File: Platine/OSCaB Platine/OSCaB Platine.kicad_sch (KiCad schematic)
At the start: 22 parts, among them IC1 TMC2209 SilentStepStick, J1 Sensor 1, J2 Sensor 2, J3 12V, J4 Motor, J5 12V, J6 io, U1 SeeeduinoXIAO ESP32C3, U2 L7805

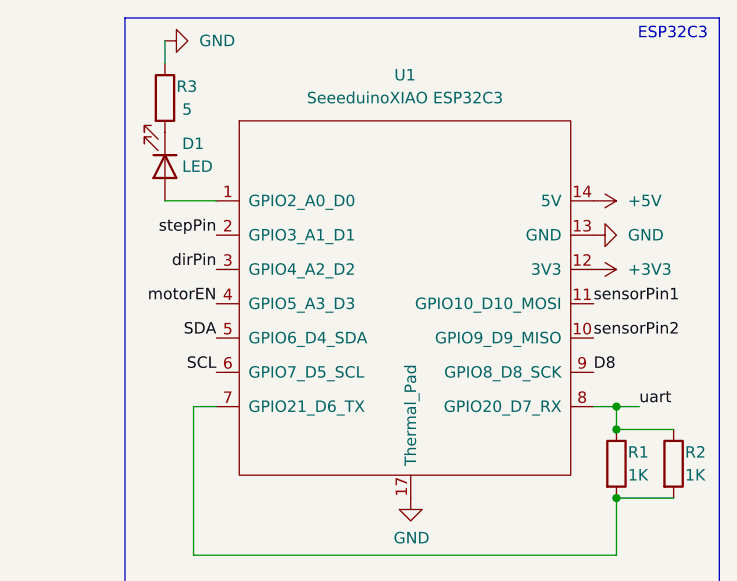
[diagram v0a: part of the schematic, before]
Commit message: PCB update
Platine auf den ESP32S3 upgedated
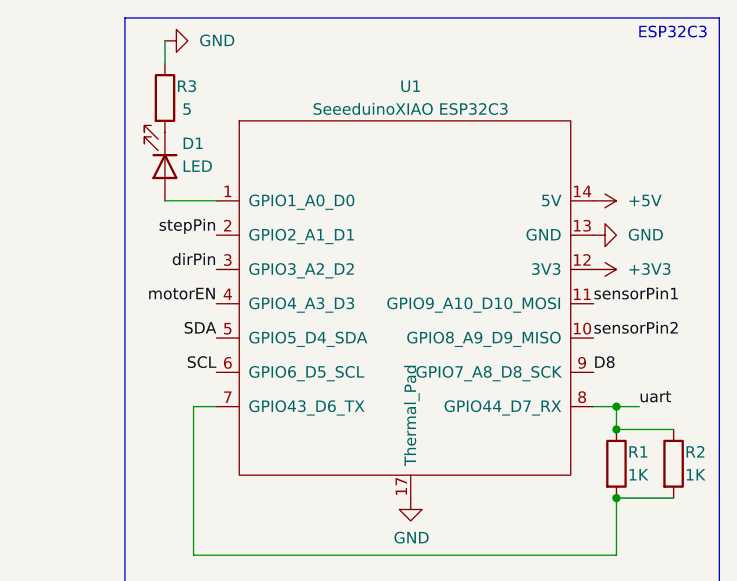
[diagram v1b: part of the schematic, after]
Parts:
- removed U1: SeeeduinoXIAO ESP32C3, Seeeduino_XIAO:Seeeduino XIAO-MOUDLE ESP32C3, symbol Seeeduino XIAO:SeeeduinoXIAO ESP32C3
- added U1: SeeeduinoXIAO ESP32C3, Seeeduino_XIAO:Seeeduino XIAO-MOUDLE ESP32S3, symbol Seeeduino XIAO:SeeeduinoXIAO ESP32S3
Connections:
- net +3V3: now also U1.12 (3V3)
- net +5V: now also U1.14 (5V)
- net D8: now also U1.9 (GPIO7_A8_D8_SCK)
- net GND: now also U1.13 (GND), U1.17 (Thermal_Pad)
- net SCL: now also U1.6 (GPIO6_D5_SCL)
- net SDA: now also U1.5 (GPIO5_D4_SDA)
- net dirPin: now also U1.3 (GPIO3_A2_D2)
- net motorEN: now also U1.4 (GPIO4_A3_D3)
- net sensorPin1: now also U1.11 (GPIO9_A10_D10_MOSI)
- net sensorPin2: now also U1.10 (GPIO8_A9_D9_MISO)
- net stepPin: now also U1.2 (GPIO2_A1_D1)
- net uart: now also U1.8 (GPIO44_D7_RX)
- net at R1.2, R2.2: now also U1.7 (GPIO43_D6_TX)
- net at D1.2 (A): now also U1.1 (GPIO1_A0_D0)
